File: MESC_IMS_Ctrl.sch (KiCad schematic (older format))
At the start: 64 parts, among them J1 Conn_01x08_Female, J2 Conn_01x08_Female, J3 Conn_01x08_Female, J4 Conn_01x06_Male, J5 Conn_ARM_JTAG_SWD_10, J6 USB_C_Receptacle_USB2.0, J7 Conn_01x03_Male, J8 Conn_01x04_Male, J9 Conn_01x08_Male, U1 STM32F303CBTx, Y1 ASE-8.000MHZ-LC-T

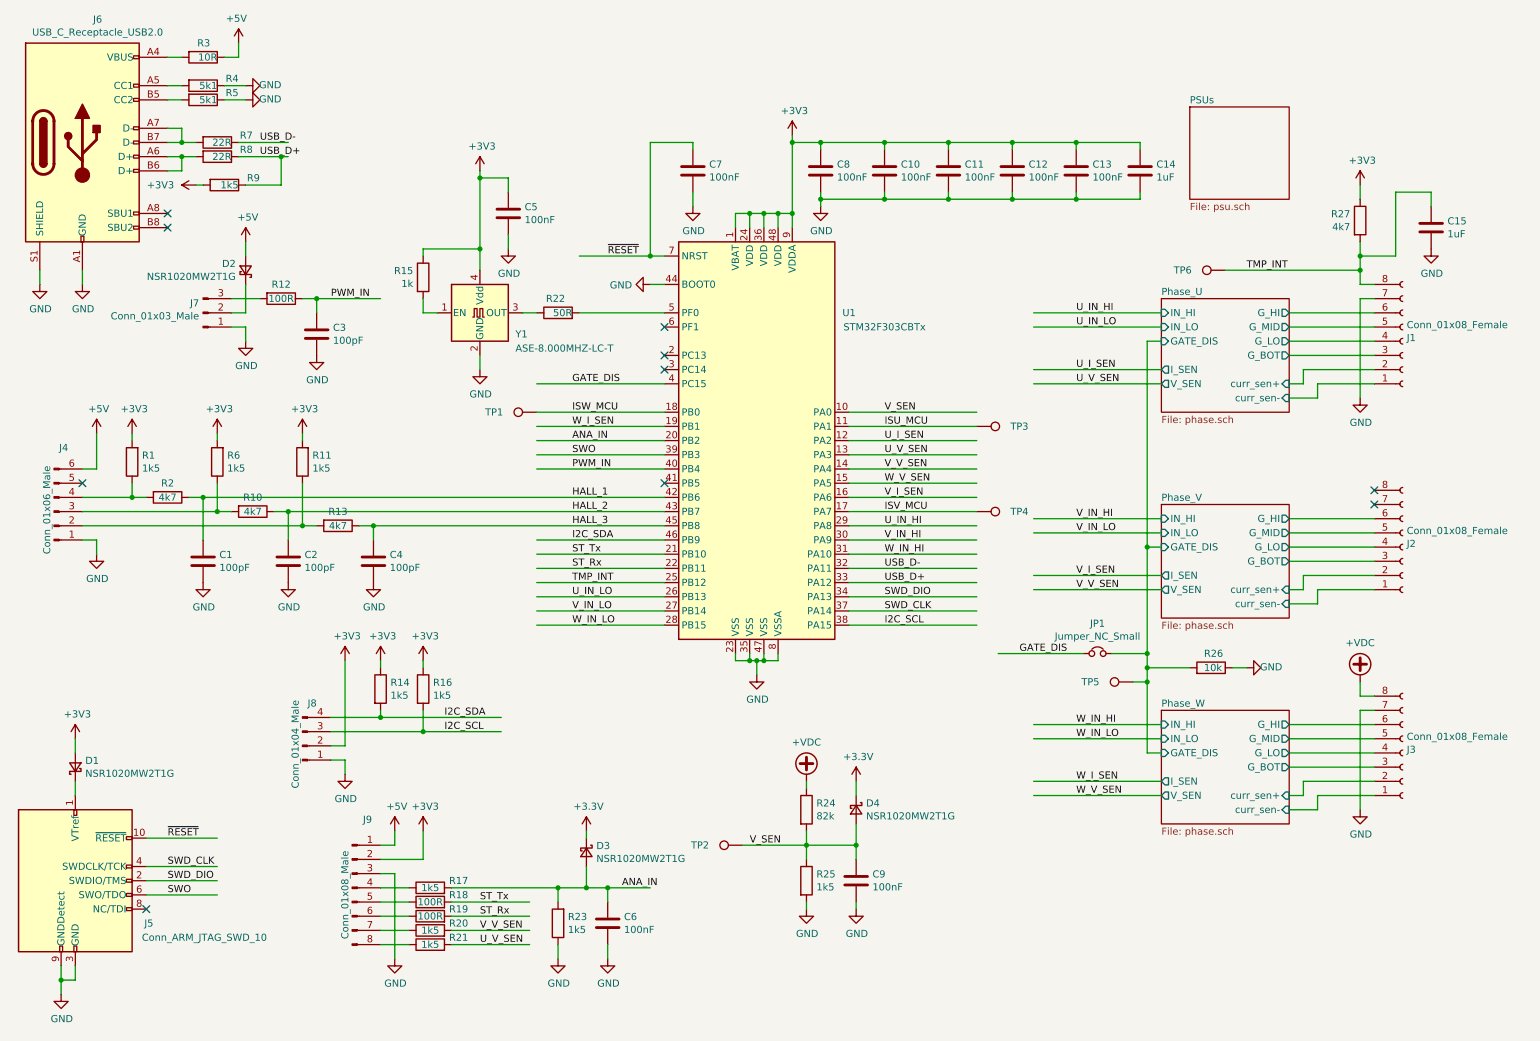
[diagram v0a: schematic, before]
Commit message: Adding low-side current comparators
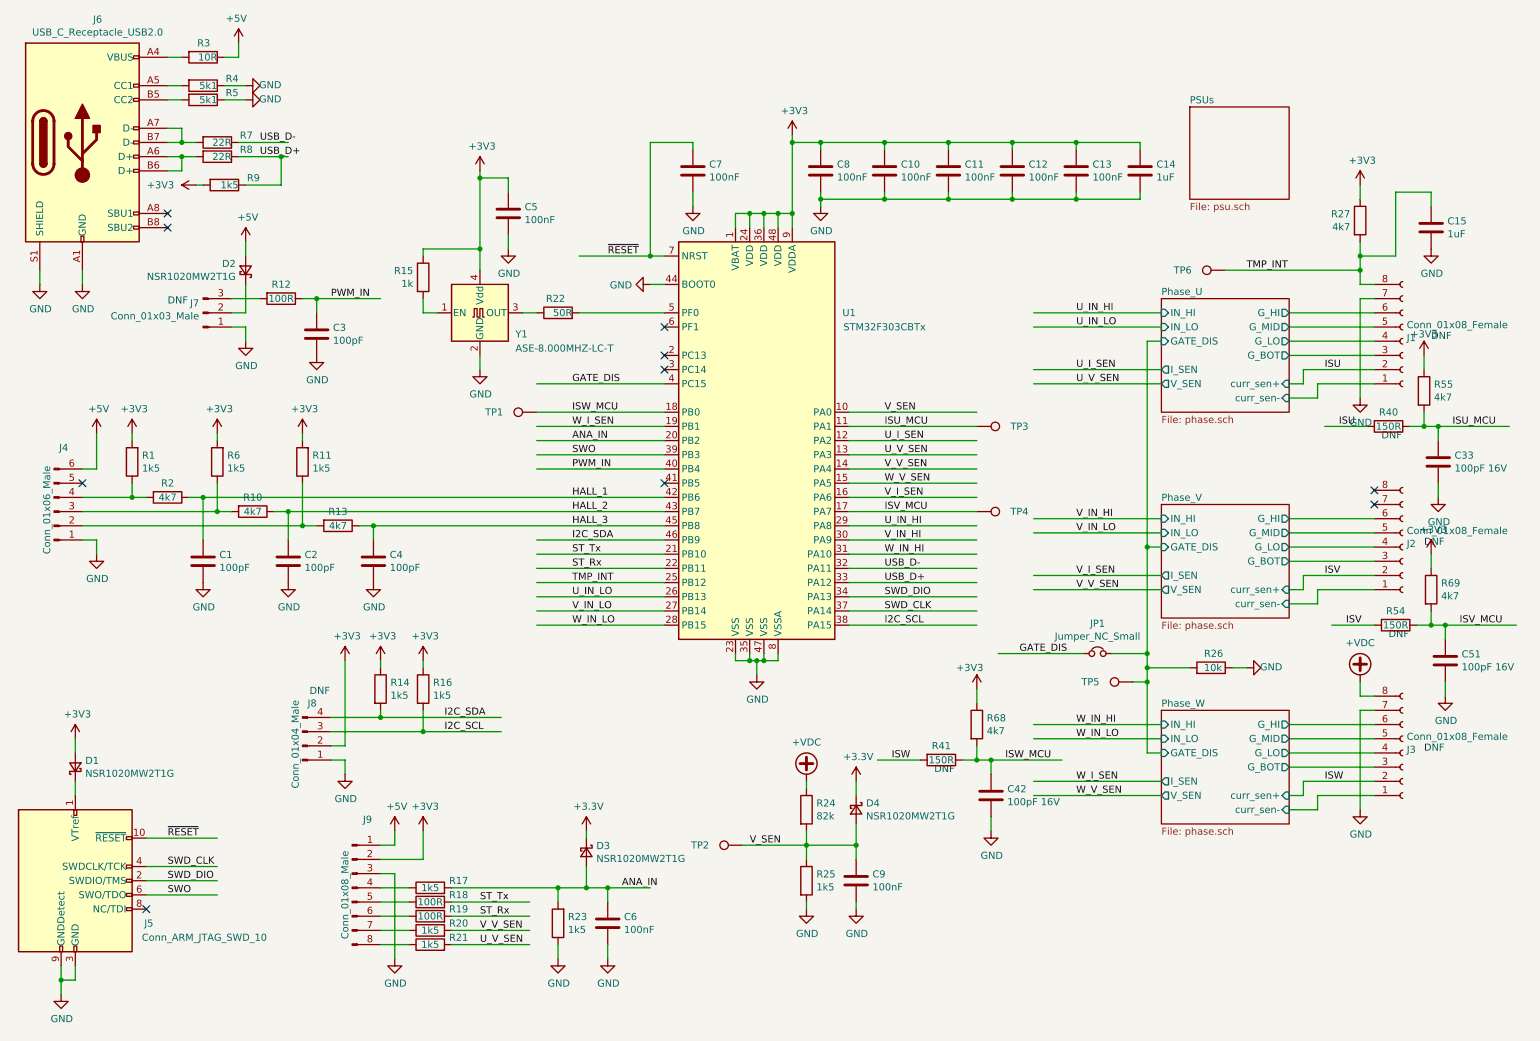
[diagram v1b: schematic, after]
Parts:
- added C33, C42, C51: 100pF 16V, Capacitor_SMD:C_0402_1005Metric, symbol Device:C
- added R40, R41, R54: 150R, Resistor_SMD:R_0402_1005Metric, symbol Device:R
- added R55, R68, R69: 4k7, Resistor_SMD:R_0402_1005Metric, symbol Device:R
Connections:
- net labels added: ISU, ISV, ISW
- wire segments 278 -> 302
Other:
- note added: "DNF"

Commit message: Adding LCSC part numbers
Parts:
- C1, C2, C3, C33, C4, C42, C51: LCSC (none) -> C1546
- C10, C11, C12, C13, C5, C6, C7, C8, C9: LCSC (none) -> C1525
- C14, C15: LCSC (none) -> C52923
- J5: LCSC (none) -> C165948
- R1, R11, R14, R16, R17, R20, R21, R23, R25, R6, R9: LCSC (none) -> C25867
- R10, R13, R2, R27, R55, R68, R69: LCSC (none) -> C25900
- R12, R18, R19: LCSC (none) -> C25076
- R15: LCSC (none) -> C11702
- R22: LCSC (none) -> C25120
- R24: LCSC (none) -> C4142
- R26: LCSC (none) -> C25744
- R3: LCSC (none) -> C25077
- R4, R5: LCSC (none) -> C25905
- R40, R41, R54: LCSC (none) -> C25082
- R7, R8: LCSC (none) -> C25092
- U1: LCSC (none) -> C108516
- Y1: LCSC (none) -> C39097

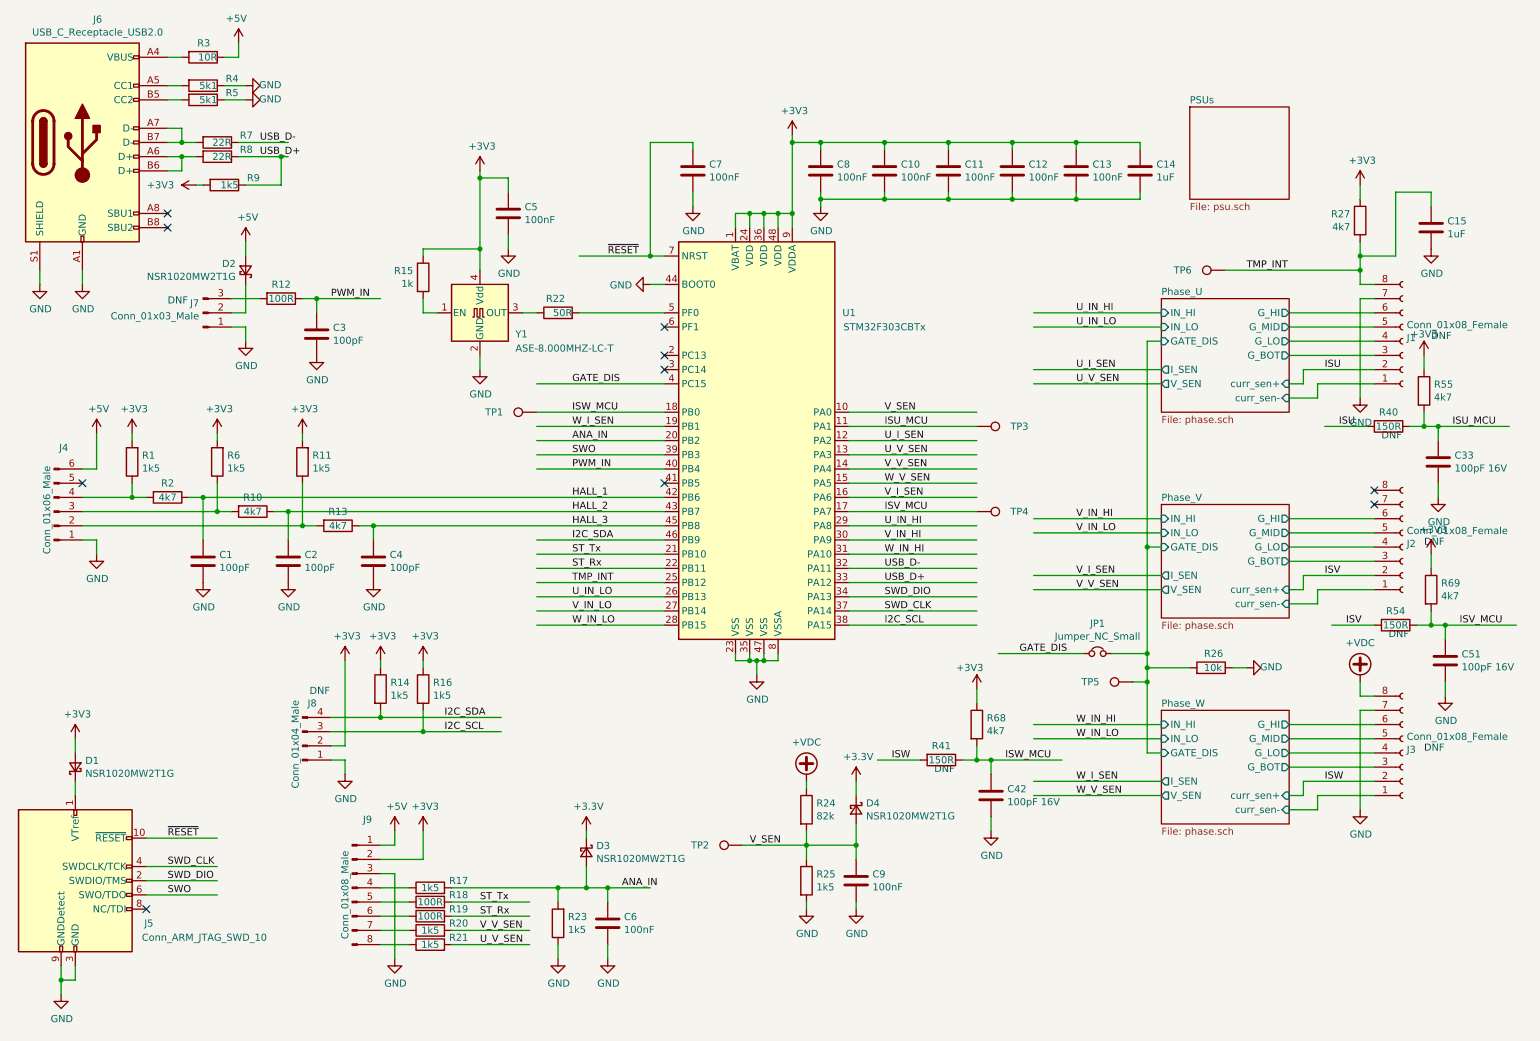
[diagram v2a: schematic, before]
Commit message: Twaeking the layout to fit into 100x100mm
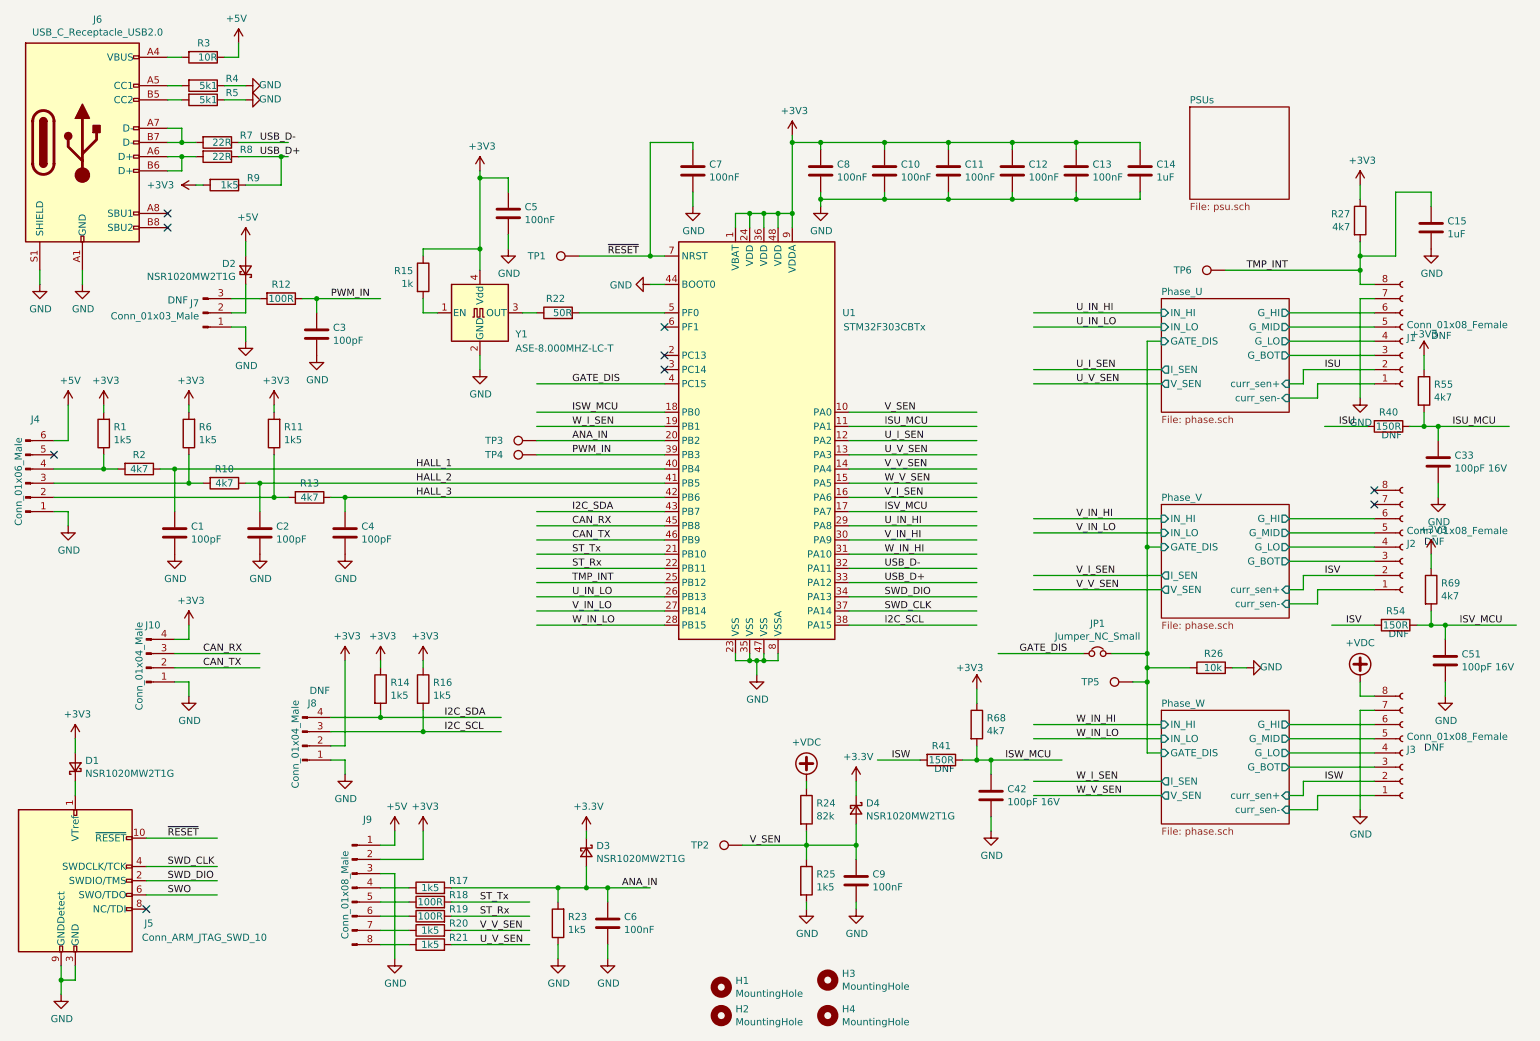
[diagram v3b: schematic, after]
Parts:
- added H1, H2, H3, H4: MountingHole, MountingHole:MountingHole_3.2mm_M3_Pad_Via, symbol Mechanical:MountingHole
- added J10: Conn_01x04_Male, Connector_PinHeader_2.54mm:PinHeader_1x04_P2.54mm_Vertical, symbol Connector:Conn_01x04_Male
- J1, J2, J3: footprint Connector_PinSocket_2.54mm:PinSocket_1x08_P2.54mm_Horizontal -> Connector_PinSocket_2.54mm:PinSocket_1x08_P2.54mm_Vertical
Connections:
- net labels added: CAN_RX, CAN_TX
- wire segments 302 -> 309
- no-connect marks 10 -> 9
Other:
- moved on the sheet: C1, C2, C4, J4, R1, R10, R11, R13, R2, R6, TP1, TP3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

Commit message: More placement
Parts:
- J4: footprint Connector_JST:JST_PH_B6B-PH-K_1x06_P2.00mm_Vertical -> Connector_JST:JST_PH_S6B-PH-SM4-TB_1x06-1MP_P2.00mm_Horizontal
- J9: footprint Connector_JST:JST_PH_B8B-PH-K_1x08_P2.00mm_Vertical -> Connector_JST:JST_PH_B8B-PH-SM4-TB_1x08-1MP_P2.00mm_Vertical
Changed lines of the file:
@@
 F 0 "J4" H 750 3400 50  0000 R CNN
 F 1 "Conn_01x06_Male" V 600 4150 50  0000 R CNN
-F 2 "Connector_JST:JST_PH_B6B-PH-K_1x06_P2.00mm_Vertical" H 650 3850 50  0001 C CNN
+F 2 "Connector_JST:JST_PH_S6B-PH-SM4-TB_1x06-1MP_P2.00mm_Horizontal" H 650 3850 50  0001 C CNN
 F 3 "~" H 650 3850 50  0001 C CNN
 F 4 "~" H 650 3850 50  0001 C CNN "LCSC"
@@
 F 0 "J9" H 3058 7181 50  0000 C CNN
 F 1 "Conn_01x08_Male" V 2900 6650 50  0000 C CNN
-F 2 "Connector_JST:JST_PH_B8B-PH-K_1x08_P2.00mm_Vertical" H 2950 6700 50  0001 C CNN
+F 2 "Connector_JST:JST_PH_B8B-PH-SM4-TB_1x08-1MP_P2.00mm_Vertical" H 2950 6700 50  0001 C CNN
 F 3 "~" H 2950 6700 50  0001 C CNN
 F 4 "~" H 2950 6700 50  0001 C CNN "LCSC"

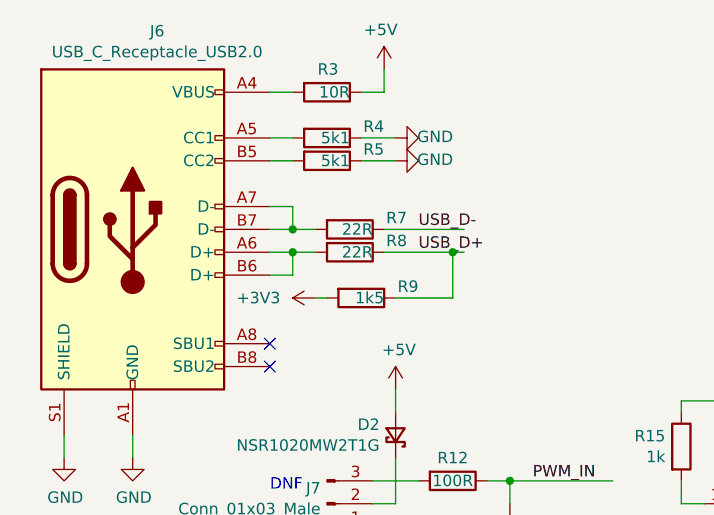
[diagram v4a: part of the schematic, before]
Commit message: Adding some basic test tracks
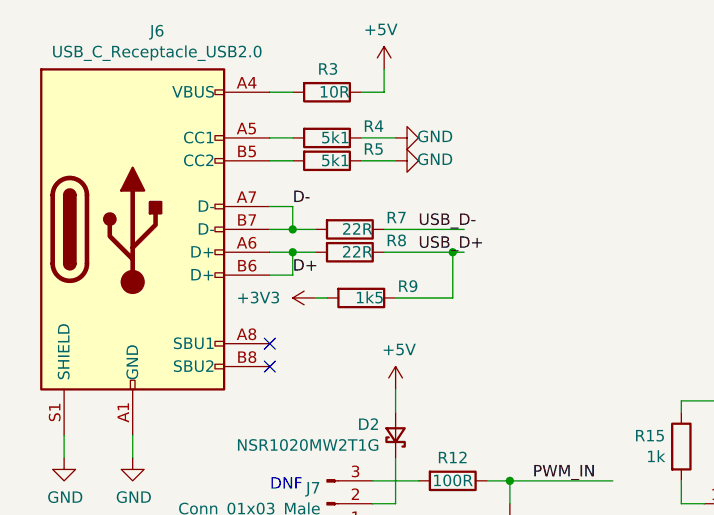
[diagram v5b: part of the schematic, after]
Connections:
- net labels added: D+, D-
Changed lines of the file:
@@
 	0    -1   -1   0
 $EndComp
+Text Label 1750 1350 0    50   ~ 0
+D-
+Text Label 1750 1650 0    50   ~ 0
+D+
 $EndSCHEMATC
